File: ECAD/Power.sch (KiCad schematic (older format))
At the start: 42 parts, among them J1 USB3_B, Q1 CJ2305, U1 AMS1117-3.3, U10 AP2127K-2.5, U4 ATtiny10-TS, U5 TPD4EUSB30, U6 TPD2EUSB30, U7 AP2127K-2.8, U9 AP2127K-1.2

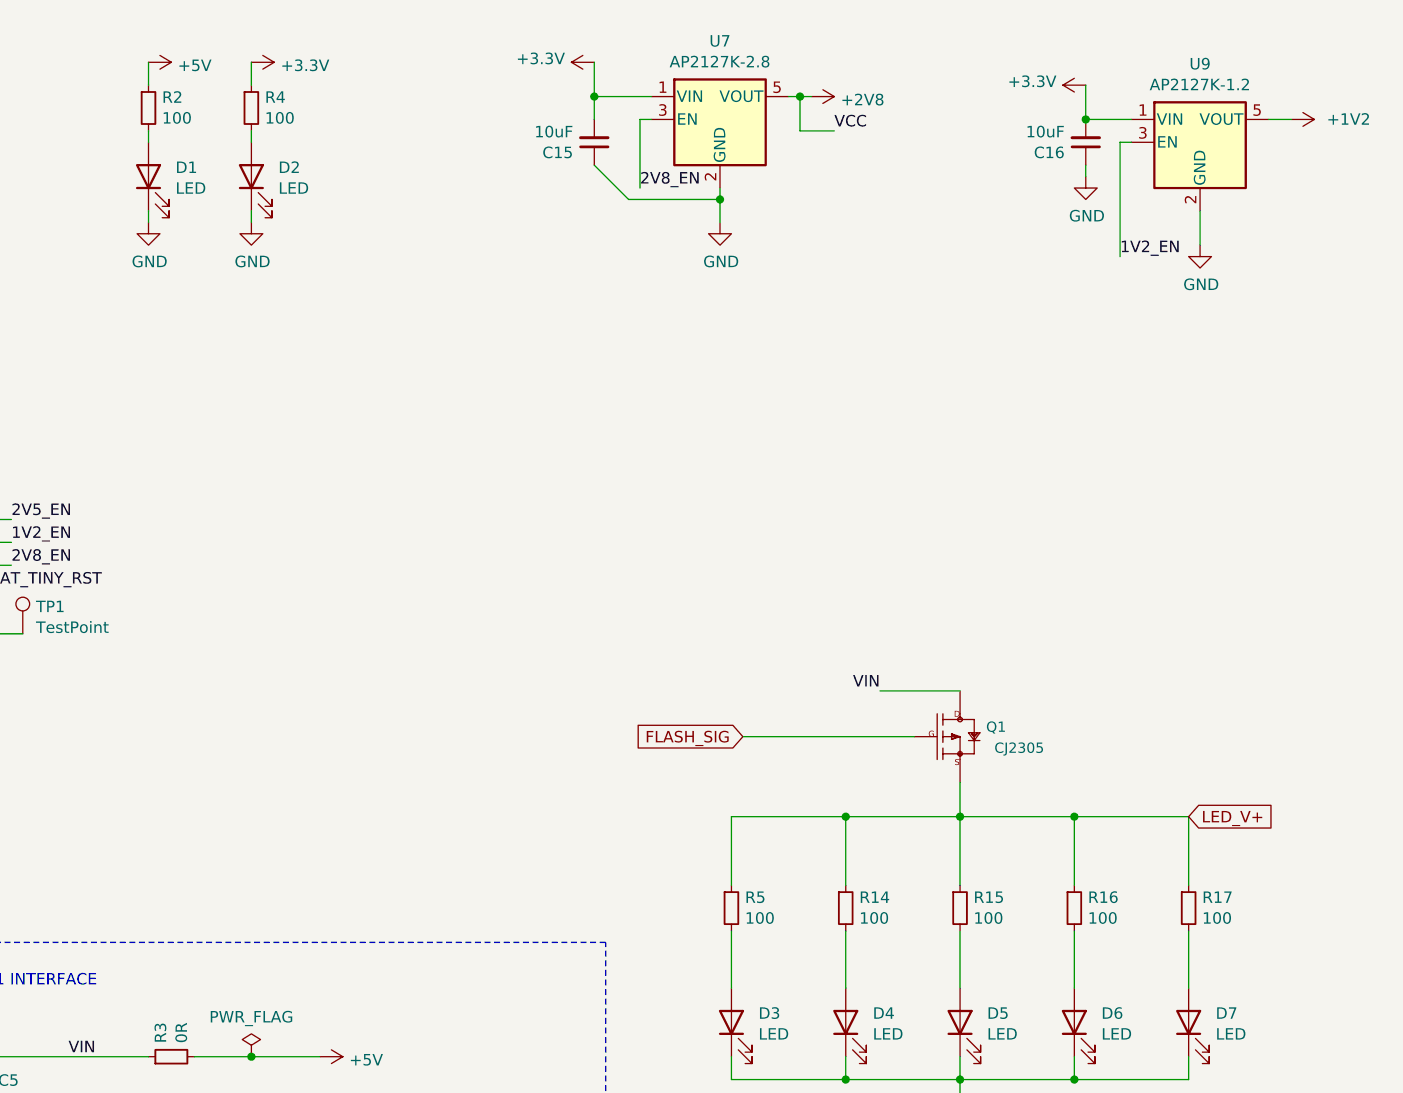
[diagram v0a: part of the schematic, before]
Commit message: Updated Crystal and LED Resistors
Updated Crystal Capacitors to 16pF and 5V series resistors for LED's to 85Ohm.
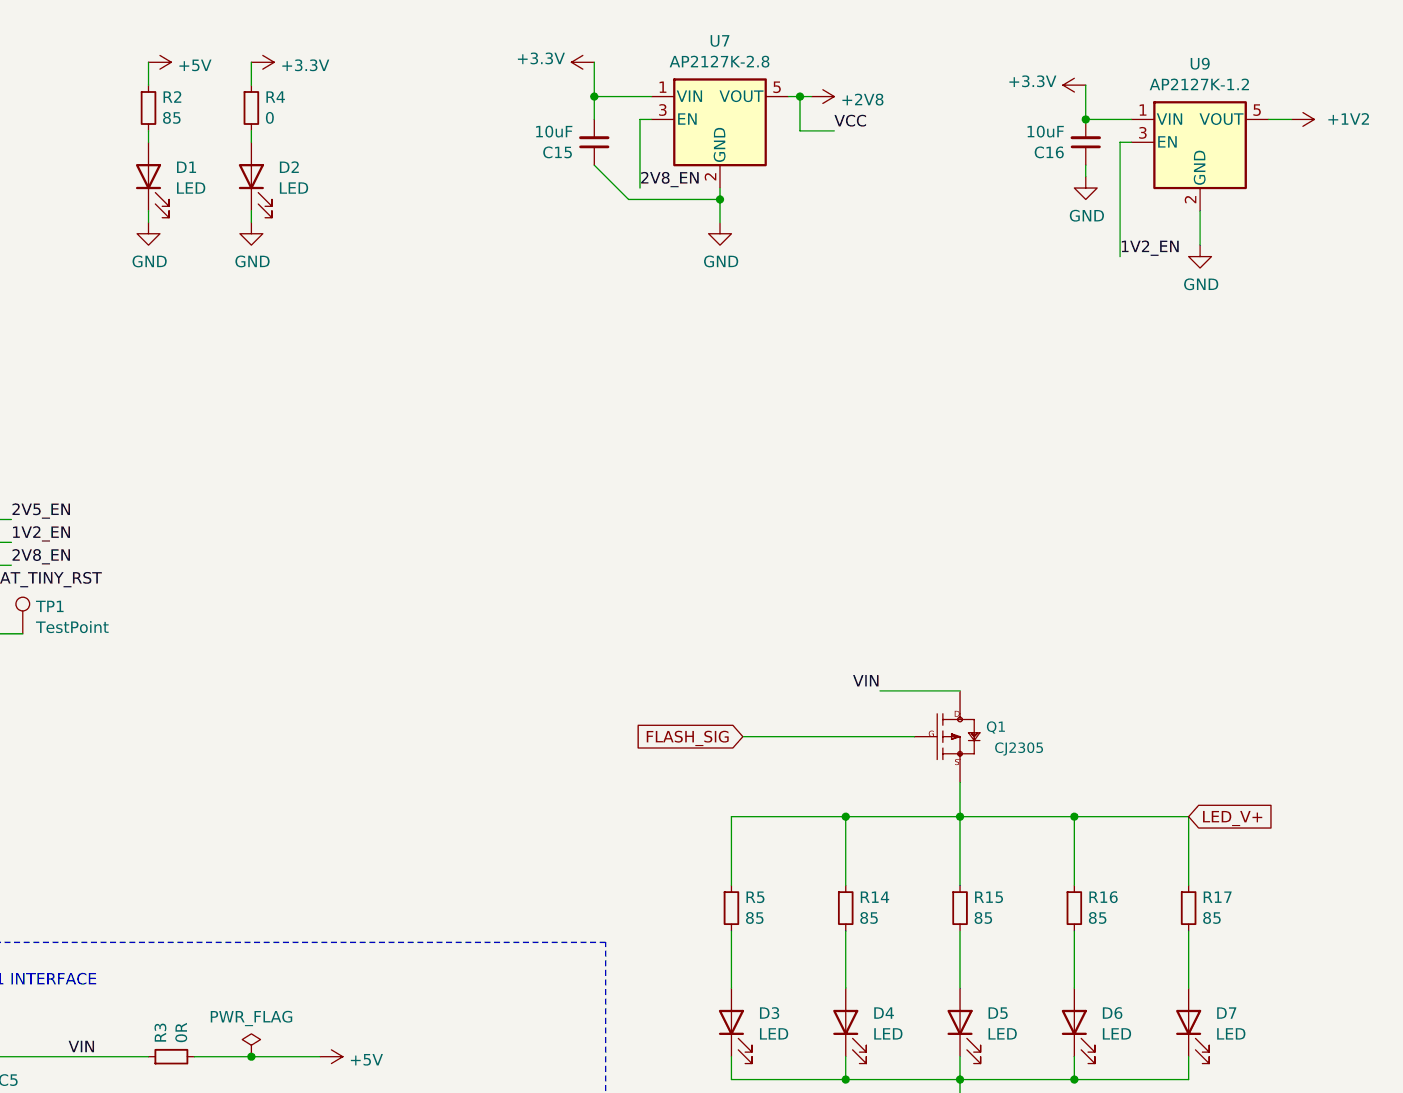
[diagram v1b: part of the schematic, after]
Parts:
- R14, R15, R16, R17, R2, R5: value 100 -> 85
- R4: value 100 -> 0
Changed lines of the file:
@@
 AR Path="/5FE173C9/60100A67" Ref="R2"  Part="1"
 F 0 "R2" H 3309 1346 50  0000 L CNN
-F 1 "100" H 3309 1255 50  0000 L CNN
+F 1 "85" H 3309 1255 50  0000 L CNN
 F 2 "Resistor_SMD:R_0805_2012Metric_Pad1.15x1.40mm_HandSolder" H 3250 1300 50  0001 C CNN
 F 3 "~" H 3250 1300 50  0001 C CNN
@@
 AR Path="/5FE173C9/60100A76" Ref="R4"  Part="1"
 F 0 "R4" H 3759 1346 50  0000 L CNN
-F 1 "100" H 3759 1255 50  0000 L CNN
+F 1 "0" H 3759 1255 50  0000 L CNN
 F 2 "Resistor_SMD:R_0805_2012Metric_Pad1.15x1.40mm_HandSolder" H 3700 1300 50  0001 C CNN
 F 3 "~" H 3700 1300 50  0001 C CNN
@@
 AR Path="/5FE173C9/603DED96" Ref="R5"  Part="1"
 F 0 "R5" H 5859 4846 50  0000 L CNN
-F 1 "100" H 5859 4755 50  0000 L CNN
+F 1 "85" H 5859 4755 50  0000 L CNN
 F 2 "Resistor_SMD:R_0805_2012Metric_Pad1.15x1.40mm_HandSolder" H 5800 4800 50  0001 C CNN
 F 3 "~" H 5800 4800 50  0001 C CNN
@@
 AR Path="/5FE173C9/603DED9D" Ref="R14"  Part="1"
 F 0 "R14" H 6359 4846 50  0000 L CNN
-F 1 "100" H 6359 4755 50  0000 L CNN
+F 1 "85" H 6359 4755 50  0000 L CNN
 F 2 "Resistor_SMD:R_0805_2012Metric_Pad1.15x1.40mm_HandSolder" H 6300 4800 50  0001 C CNN
 F 3 "~" H 6300 4800 50  0001 C CNN
@@
 AR Path="/5FE173C9/603DEDA4" Ref="R15"  Part="1"
 F 0 "R15" H 6859 4846 50  0000 L CNN
-F 1 "100" H 6859 4755 50  0000 L CNN
+F 1 "85" H 6859 4755 50  0000 L CNN
 F 2 "Resistor_SMD:R_0805_2012Metric_Pad1.15x1.40mm_HandSolder" H 6800 4800 50  0001 C CNN
 F 3 "~" H 6800 4800 50  0001 C CNN
@@
 AR Path="/5FE173C9/603DEDAB" Ref="R16"  Part="1"
 F 0 "R16" H 7359 4846 50  0000 L CNN
-F 1 "100" H 7359 4755 50  0000 L CNN
+F 1 "85" H 7359 4755 50  0000 L CNN
 F 2 "Resistor_SMD:R_0805_2012Metric_Pad1.15x1.40mm_HandSolder" H 7300 4800 50  0001 C CNN
 F 3 "~" H 7300 4800 50  0001 C CNN
@@
 AR Path="/5FE173C9/603DEDBA" Ref="R17"  Part="1"
 F 0 "R17" H 7859 4846 50  0000 L CNN
-F 1 "100" H 7859 4755 50  0000 L CNN
+F 1 "85" H 7859 4755 50  0000 L CNN
 F 2 "Resistor_SMD:R_0805_2012Metric_Pad1.15x1.40mm_HandSolder" H 7800 4800 50  0001 C CNN
 F 3 "~" H 7800 4800 50  0001 C CNN

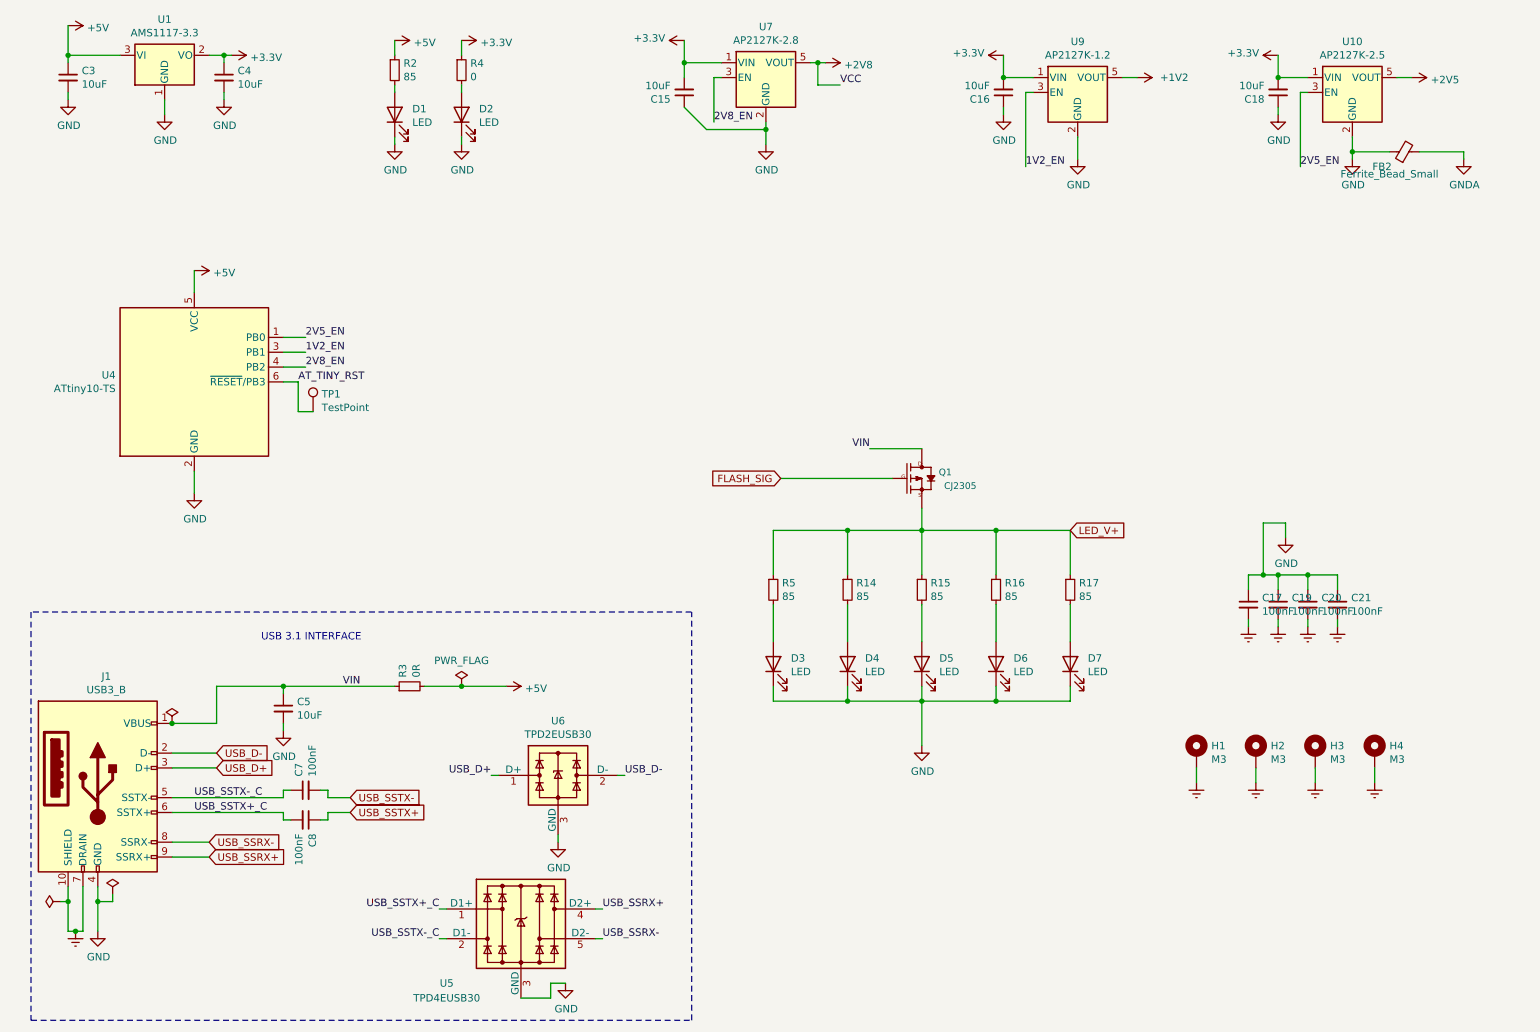
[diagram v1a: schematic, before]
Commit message: Creation of Rev003
Creation of Rev003. This is a mini-sized board for easier fitment into tight spaces. The USB connector has changed to a USB Type-C. Some components have changed footprint to 0402.
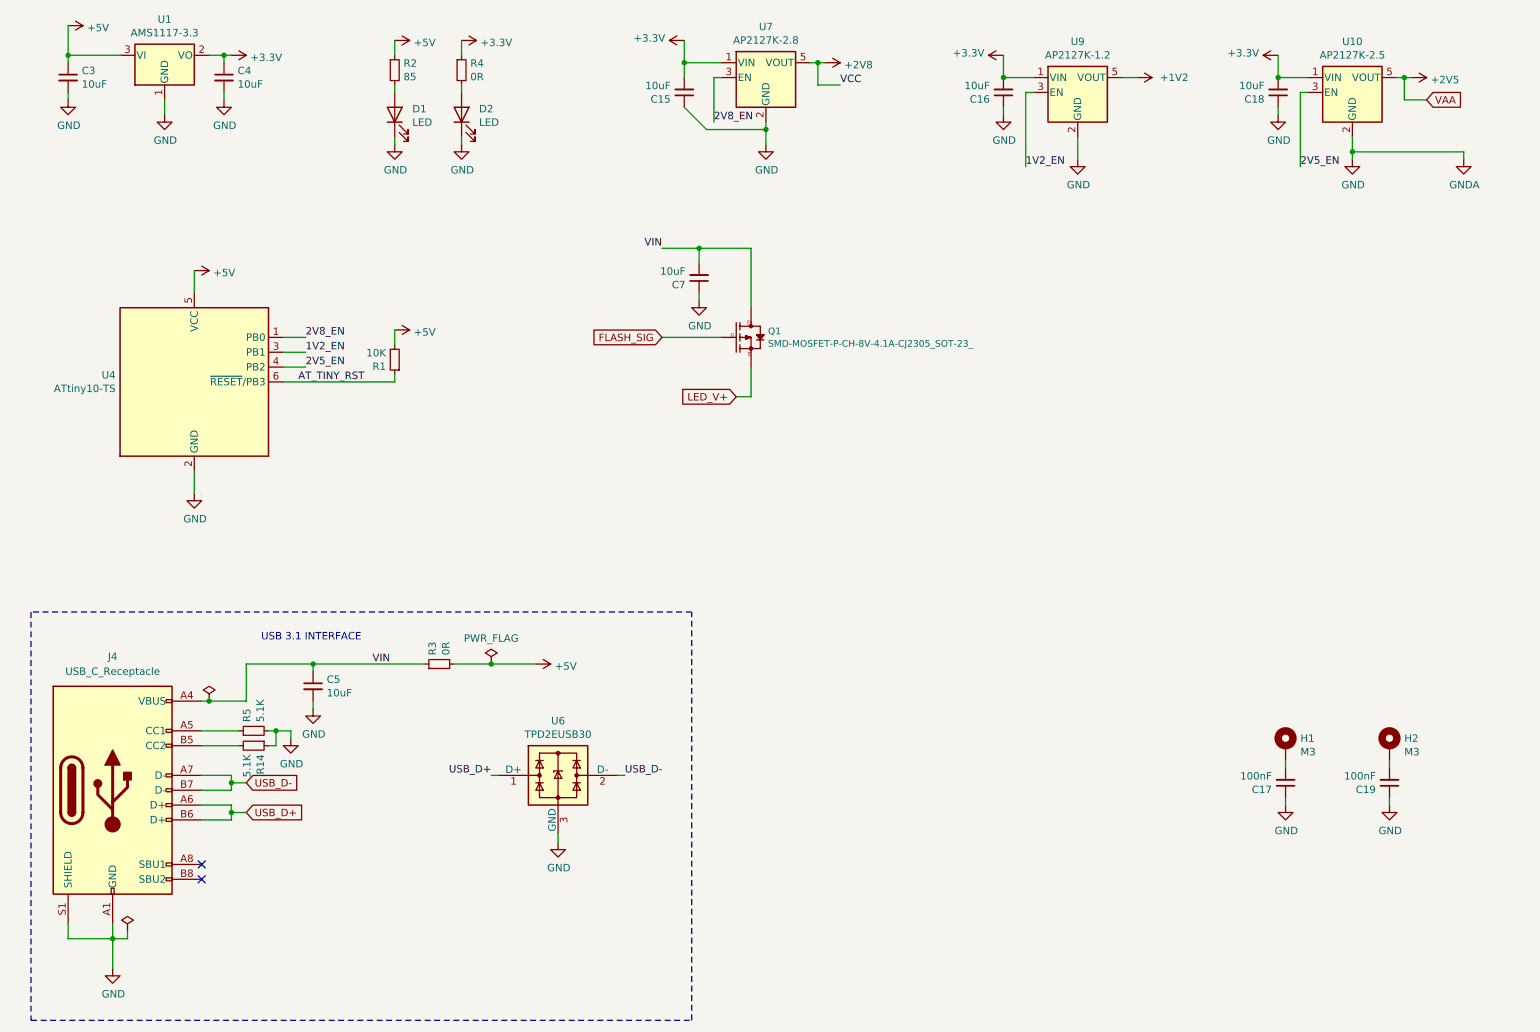
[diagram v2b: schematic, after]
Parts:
- removed C20, C21, C8: 100nF, Capacitor_SMD:C_0402_1005Metric, symbol Device:C_Small
- removed D3, D4, D5, D6, D7: LED, LED_SMD:LED_1210_3225Metric_Pad1.42x2.65mm_HandSolder, symbol Device:LED
- removed FB2: Ferrite_Bead_Small, Resistor_SMD:R_0805_2012Metric_Pad1.15x1.40mm_HandSolder, symbol Device:Ferrite_Bead_Small
- removed H3, H4: M3, MountingHole:MountingHole_3.2mm_M3_Pad_Via, symbol Mechanical:MountingHole_Pad
- removed J1: USB3_B, OpenPnPVis:U235-091N-4BLRC16-4-5, symbol Connector:USB3_B
- removed R15, R16, R17: 85, Resistor_SMD:R_0805_2012Metric_Pad1.15x1.40mm_HandSolder, symbol Device:R_Small
- removed TP1: TestPoint, TestPoint:TestPoint_Loop_D1.80mm_Drill1.0mm_Beaded, symbol Connector:TestPoint
- removed U5: TPD4EUSB30, Package_SON:USON-10_2.5x1.0mm_P0.5mm, symbol Power_Protection:TPD4EUSB30
- added J4: USB_C_Receptacle, Type-C:HRO-TYPE-C-31-M-12-Assembly, symbol Connector:USB_C_Receptacle_USB2.0
- added R1: 10K, Resistor_SMD:R_0402_1005Metric, symbol Device:R_Small
- C15, C16, C18, C3, C4, C5: MPN (none) -> CL21A106KOQNNNE
- C17, C19: MPN (none) -> CC0402KRX7R7BB104
- C7: value 100nF -> 10uF; footprint Capacitor_SMD:C_0402_1005Metric -> Capacitor_SMD:C_0805_2012Metric_Pad1.15x1.40mm_HandSolder; MPN (none) -> CL21A106KOQNNNE
- D1, D2: MPN (none) -> ORH-B35A
- H1, H2: footprint MountingHole:MountingHole_3.2mm_M3_Pad_Via -> MountingHole:MountingHole_2.2mm_M2_Pad_Via; MPN (none) -> N/A
- Q1: value CJ2305 -> SMD-MOSFET-P-CH-8V-4.1A-CJ2305_SOT-23_
- R14, R5: value 85 -> 5.1K; footprint Resistor_SMD:R_0805_2012Metric_Pad1.15x1.40mm_HandSolder -> Resistor_SMD:R_0402_1005Metric; MPN (none) -> RC0402FR-075K1L
- R2: footprint Resistor_SMD:R_0805_2012Metric_Pad1.15x1.40mm_HandSolder -> Resistor_SMD:R_0402_1005Metric; MPN (none) -> RC0402FR-0785RL
- R3: footprint Resistor_SMD:R_0805_2012Metric_Pad1.15x1.40mm_HandSolder -> Resistor_SMD:R_0402_1005Metric; MPN RC0805FR-070RL -> RC0402FR-070RL
- R4: value 0 -> 0R; footprint Resistor_SMD:R_0805_2012Metric_Pad1.15x1.40mm_HandSolder -> Resistor_SMD:R_0402_1005Metric; MPN (none) -> RC0402FR-070RL
- U10: MPN (none) -> AP2127K-2.5
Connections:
- net USB_SSTX- is gone; now on net VIN: C7.2
- net USB_SSTX-_C is gone; now on net GND: C7.1
- net +5V: now also R1.2
- net 2V5_EN: now also U4.4 (PB2); no longer U4.1 (PB0)
- net 2V8_EN: now also U4.1 (PB0); no longer U4.4 (PB2)
- net AT_TINY_RST: now also R1.1
- net GND: now also R14.1, R5.2, J4.A1 (GND), J4.A12 (GND), J4.B1 (GND), J4.B12 (GND), J4.S1 (SHIELD)
- net LED_V+: no longer R14.1, R5.1
- net USB_D+: now also J4.A6 (D+), J4.B6 (D+)
- net USB_D-: now also J4.A7 (D-), J4.B7 (D-)
- net VIN: now also J4.A4 (VBUS), J4.A9 (VBUS), J4.B4 (VBUS), J4.B9 (VBUS)
- net at R14.2: now also J4.B5 (CC2)
- net Earth: no longer names the net of C19.2, H2.1
- net Earth: no longer C17.2, H1.1
- new net: J4.A5 (CC1), R5.1
- new net: C17.2, H1.1
- no-connect marks 0 -> 2
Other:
- moved on the sheet: C17, C19, C5, H1, H2, R3
